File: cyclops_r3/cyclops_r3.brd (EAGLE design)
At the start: 124.5 x 79.9 mm, 123 parts, among them Q1 BC817, Q2 IRF510, U1 MCP4921, U10 LMP7707, U11 ZXTD45, U12 ZXTD45, U2 ADG3301, U3 MCP4022-50k, U4 317-N, U5 TLV3701, U6 337-N, U7 ADR03, U8 OP1177, U9 TLV2374, X1 SLP3, X2 SLP3, X3 SLP3

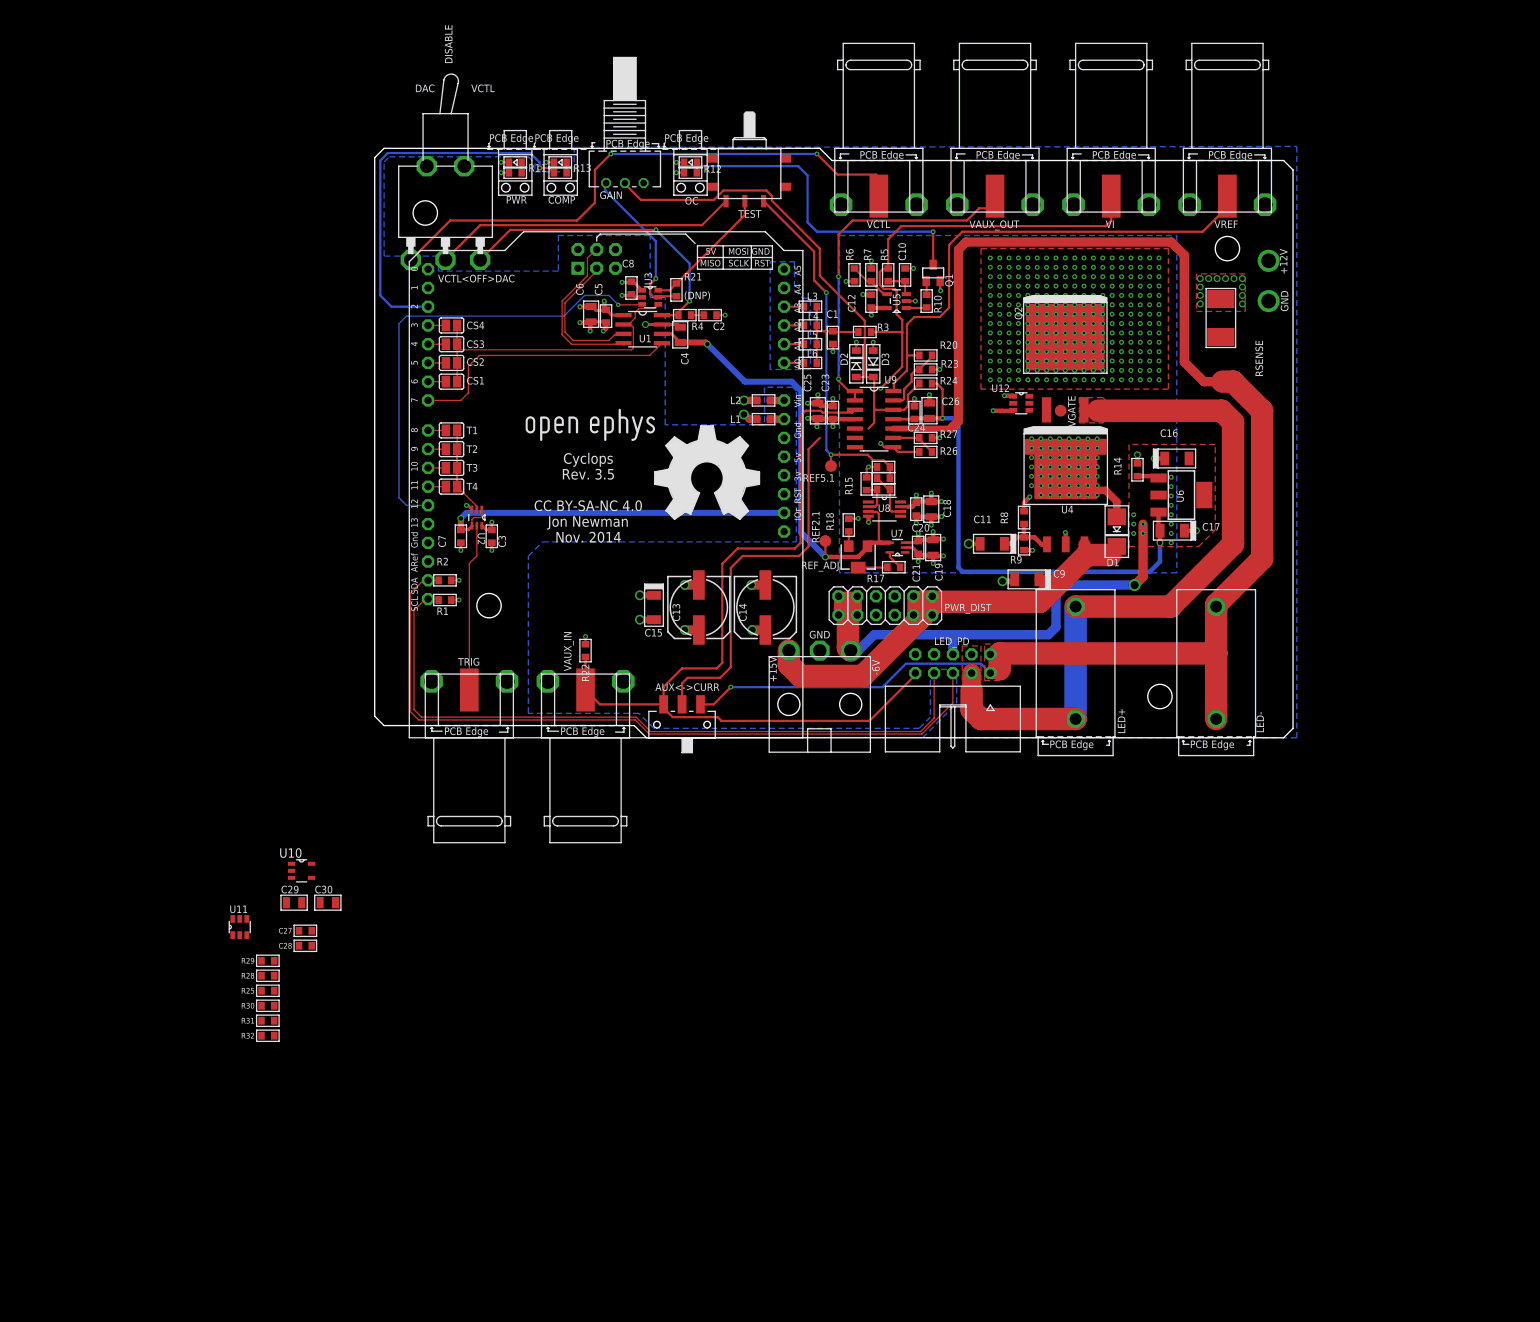
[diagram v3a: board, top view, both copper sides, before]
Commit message: Implemented new negative rail on schematic.
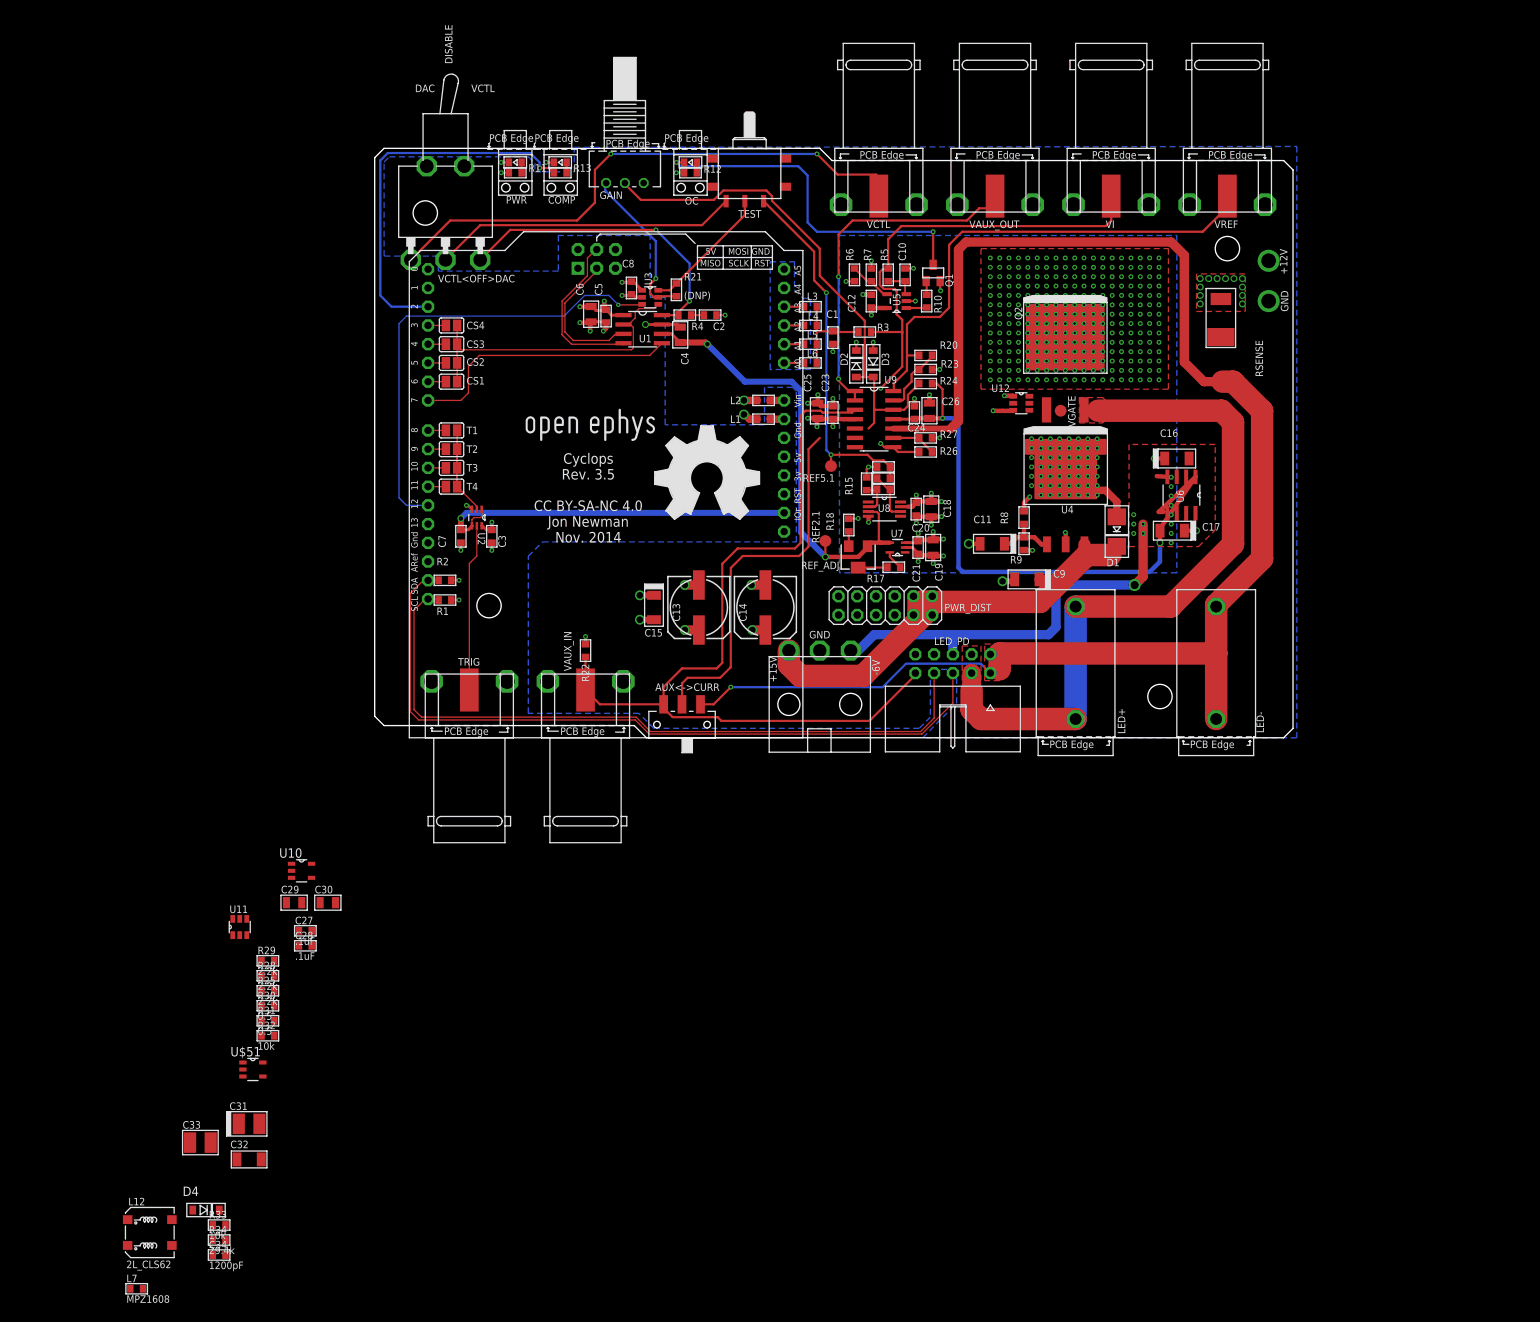
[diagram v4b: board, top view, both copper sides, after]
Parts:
- removed R14: 0, cyclops:0603
- added C31: 22uF, cyclops:1210-POL
- added C32: 1uF, cyclops:1206
- added C33: 22uF, cyclops:1210
- added C34: 1200pF, cyclops:0603
- added D4: MBR0520L, cyclops:SOD123
- added L12: 2L_CLS62, cyclops:CLS62
- added L7: MPZ1608, cyclops:0603
- added R33: 10k, cyclops:0603
- added R34: 29.4k, cyclops:0603
- added U$51: LT1611, cyclops:SOT95P310X175-5N
- U6: value 337-N -> 337L; device cyclops:SOT223 -> cyclops:SOIC127P600X175-8N
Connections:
- removed net -6V: C16.-, LED_PD.5, PWR_DIST.10, PWR_DIST.11, PWR_DIST.12, PWR_DIST.9, PWR_IN.3, U6.4
- removed net N$12: R14.1, U6.1
- new net -5V: C16.-, L7.2, LED_PD.5, U6.2, U6.3, U6.6, U6.7
- new net N$32: C32.1, L12.1, U$51.1
- new net N$33: C32.2, D4.A, L12.2
- new net N$35: C33.1, C34.1, L12.3, L7.1, R34.2
- new net N$36: C34.2, R33.2, R34.1, U$51.3
- new net VIN: C31.+, L12.4, U$51.4, U$51.5
- net -1.25V: now also U6.1; no longer U6.3
- net GND: now also C31.-, C33.2, D4.C, R33.1, U$51.2, U6.4; no longer R14.2
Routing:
- net -6V: track 79.6 -> 0.00 mm, vias 14 -> 0
- net -5V: track 0.00 -> 55.2 mm, vias 0 -> 14
- net -1.25V: track 73.2 -> 86.4 mm
- net N$12: track 2.97 -> 0.00 mm
- net GND: track 111.4 -> 111.7 mm, vias 57 -> 56
- added copper zone on layer 1, net -5V
- removed copper zone on layer 1, net -6V

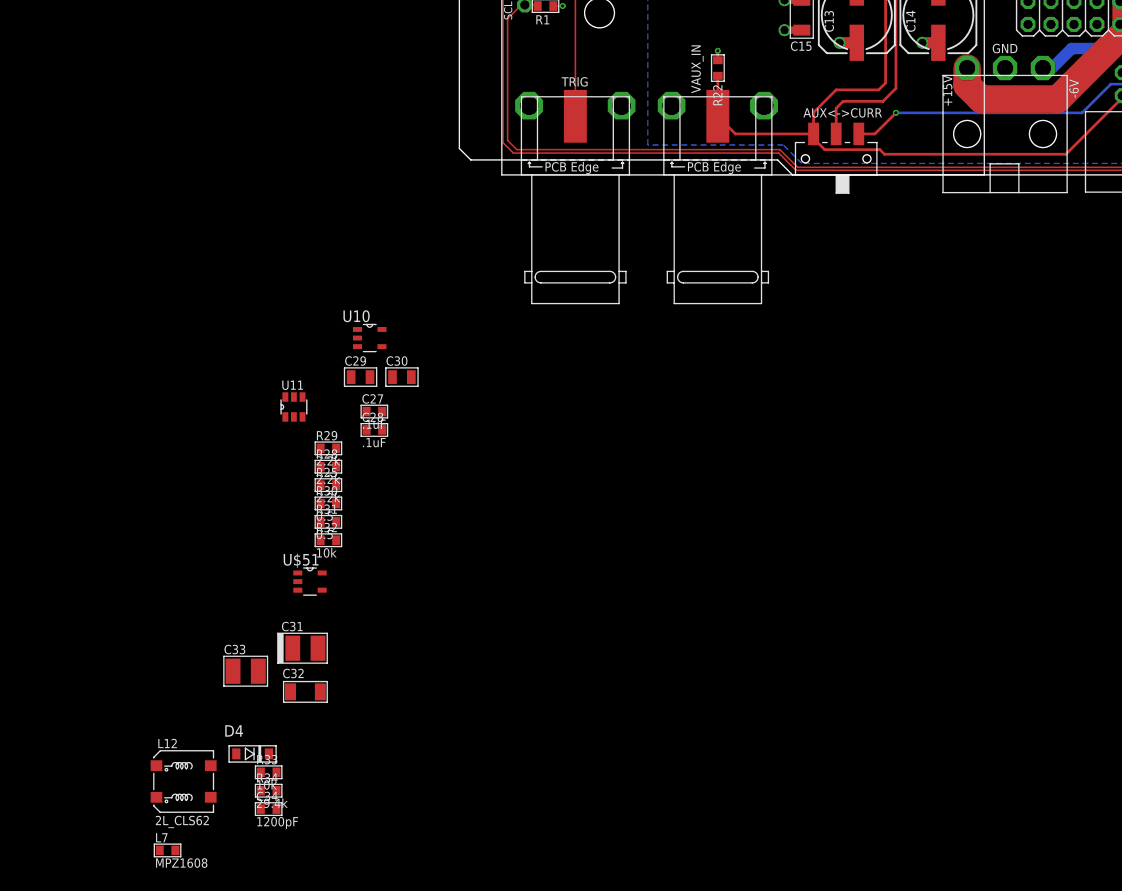
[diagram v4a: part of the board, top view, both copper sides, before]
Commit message: New schematic should be finished. Double check and then layout board.
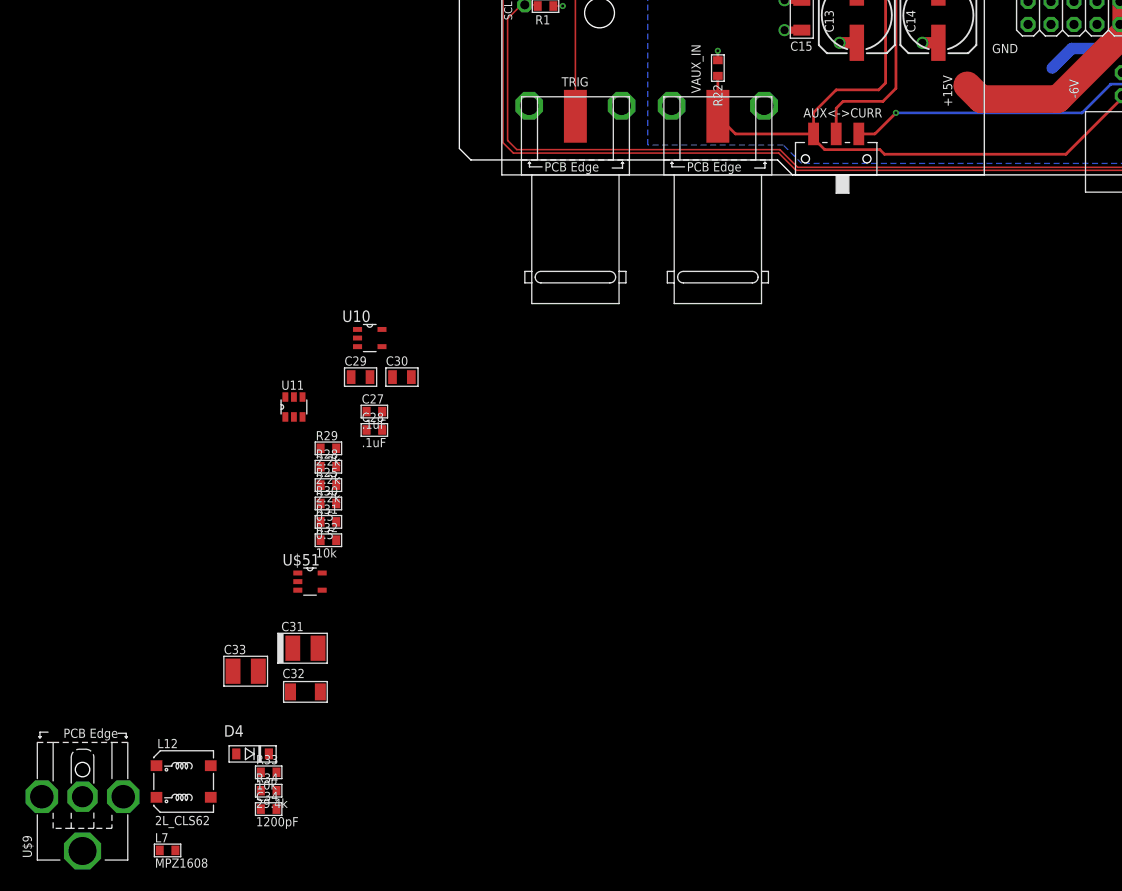
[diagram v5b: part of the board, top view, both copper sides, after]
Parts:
- removed PWR_IN: PINH1X3_MINI-JR, cyclops:MINI-JR-1X3
- added U$9: BARREL-JACK_PJ-063BH, cyclops:PJ-063BH
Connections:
- net +15V: now also U$9.1; no longer PWR_IN.1
- net GND: now also U$9.2; no longer PWR_IN.2
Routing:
- net +15V: track 69.4 -> 67.5 mm
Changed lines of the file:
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@@
 <attribute name="VALUE" x="77.216" y="18.542" size="1.016" layer="27" font="vector" ratio="18"/>
 </element>
-<element name="PWR_IN" library="cyclops" package="MINI-JR-1X3" value="PINH1X3_MINI-JR" x="56.134" y="4.5212" smashed="yes"/>
 <element name="GAIN" library="cyclops" package="3310C-001" value="1k" x="33.909" y="75.184" smashed="yes" rot="R90">
 <attribute name="NAME" x="30.48" y="73.025" size="1.016" layer="25" font="vector" ratio="18"/>
@@
 <element name="L12" library="cyclops" package="CLS62" value="2L_CLS62" x="-30.48" y="-67.056"/>
 <element name="L7" library="cyclops" package="0603" value="MPZ1608" x="-32.258" y="-74.676"/>
+<element name="U$9" library="cyclops" package="PJ-063BH" value="BARREL-JACK_PJ-063BH" x="-41.656" y="-62.738"/>
 </elements>
 <signals>
@@
 <contactref element="VCTL" pad="3"/>
 <contactref element="VCTL" pad="2"/>
-<contactref element="PWR_IN" pad="2"/>
 <contactref element="GAIN" pad="1"/>
 <polygon width="0.254" layer="2" thermals="no" rank="3">
@@
 <contactref element="U6" pad="4"/>
 <wire x1="105.9872" y1="35.4584" x2="107.435" y2="35.3568" width="0.6096" layer="1"/>
+<contactref element="U$9" pad="2"/>
 <wire x1="110.45825" y1="72.2376" x2="120.68175" y2="72.2376" width="0" layer="19" extent="1-1"/>
 <wire x1="104.93375" y1="72.2376" x2="110.45825" y2="72.2376" width="0" layer="19" extent="1-1"/>
@@
 <wire x1="73.279" y1="11.303" x2="70.485" y2="16.637" width="0" layer="19" extent="1-1"/>
 <wire x1="63.21425" y1="72.2376" x2="67.31" y2="64.643" width="0" layer="19" extent="1-1"/>
-<wire x1="60.325" y1="11.811" x2="67.945" y2="16.637" width="0" layer="19" extent="1-1"/>
-<wire x1="52.95" y1="20.701" x2="60.325" y2="11.811" width="0" layer="19" extent="1-1"/>
-<wire x1="43.935" y1="20.703" x2="51.054" y2="20.701" width="0" layer="19" extent="1-1"/>
-<wire x1="37.853" y1="16.002" x2="42.037" y2="20.701" width="0" layer="19" extent="1-1"/>
-<wire x1="33.68675" y1="7.6454" x2="35.941" y2="16.002" width="0" layer="19" extent="1-1"/>
-<wire x1="23.46325" y1="7.6454" x2="33.68675" y2="7.6454" width="0" layer="19" extent="1-1"/>
-<wire x1="17.93875" y1="7.6454" x2="23.46325" y2="7.6454" width="0" layer="19" extent="1-1"/>
-<wire x1="7.71525" y1="7.6454" x2="17.93875" y2="7.6454" width="0" layer="19" extent="1-1"/>
 <wire x1="47.498" y1="57.277" x2="50.038" y2="43.815" width="0" layer="19" extent="1-1"/>
 <wire x1="41.409" y1="55.6514" x2="46.3226" y2="57.277" width="0" layer="19" extent="1-1"/>
@@
 <wire x1="24.2824" y1="77.978" x2="36.449" y2="75.184" width="0" layer="19" extent="1-1"/>
 <wire x1="18.1864" y1="77.978" x2="22.098" y2="79.248" width="0" layer="19" extent="1-2"/>
+<wire x1="52.95" y1="20.701" x2="64.255" y2="29.6926" width="0" layer="19" extent="1-1"/>
+<wire x1="43.935" y1="20.703" x2="51.054" y2="20.701" width="0" layer="19" extent="1-1"/>
+<wire x1="37.853" y1="16.002" x2="42.037" y2="20.701" width="0" layer="19" extent="1-1"/>
+<wire x1="33.68675" y1="7.6454" x2="35.941" y2="16.002" width="0" layer="19" extent="1-1"/>
+<wire x1="23.46325" y1="7.6454" x2="33.68675" y2="7.6454" width="0" layer="19" extent="1-1"/>
+<wire x1="17.93875" y1="7.6454" x2="23.46325" y2="7.6454" width="0" layer="19" extent="1-1"/>
+<wire x1="7.71525" y1="7.6454" x2="17.93875" y2="7.6454" width="0" layer="19" extent="1-1"/>
 <wire x1="15.875" y1="25.4" x2="17.93875" y2="7.6454" width="0" layer="19" extent="1-1"/>
 <wire x1="11.684" y1="25.4" x2="15.875" y2="25.4" width="0" layer="19" extent="1-1"/>
@@
 <wire x1="-21.06" y1="-64.008" x2="-22.225" y2="-54.864" width="0" layer="19" extent="1-1"/>
 <wire x1="-21.9456" y1="-66.04" x2="-21.06" y2="-64.008" width="0" layer="19" extent="1-1"/>
+<wire x1="-41.656" y1="-68.738" x2="-21.9456" y2="-66.04" width="0" layer="19" extent="1-1"/>
 </signal>
 <signal name="N$1">
@@
 <contactref element="D1" pad="C"/>
 <contactref element="C9" pad="+"/>
-<contactref element="PWR_IN" pad="1"/>
 <wire x1="96.266" y1="26.1423" x2="96.1955" y2="26.2128" width="1.016" layer="1"/>
 <contactref element="PWR_DIST" pad="1"/>
@@
 <wire x1="66.162021875" y1="8.382" x2="57.658" y2="8.382" width="3.048" layer="1"/>
 <wire x1="57.658" y1="8.382" x2="56.134" y2="9.906" width="3.048" layer="1"/>
-<wire x1="56.134" y1="9.906" x2="56.134" y2="11.811" width="3.048" layer="1"/>
 <wire x1="66.162021875" y1="8.382" x2="74.93" y2="17.149978125" width="3.048" layer="1"/>
 <wire x1="74.93" y1="17.149978125" x2="74.93" y2="18.415" width="3.048" layer="1"/>
+<contactref element="U$9" pad="1"/>
+<wire x1="56.134" y1="9.906" x2="-41.656" y2="-74.738" width="0" layer="19" extent="1-1"/>
 </signal>
 <signal name="LED+">
